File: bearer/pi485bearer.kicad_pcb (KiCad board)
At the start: 2 copper layers, 70 x 30 mm, 23 parts, among them P1 PWR, P2 Rasperry Pi, P3 RO, P4 TERM, P5 CONN_01X04, P6 CONN_01X04, Q1 2N3904, Q2 2N3904, Q3 2N3904, Q4 2N3906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

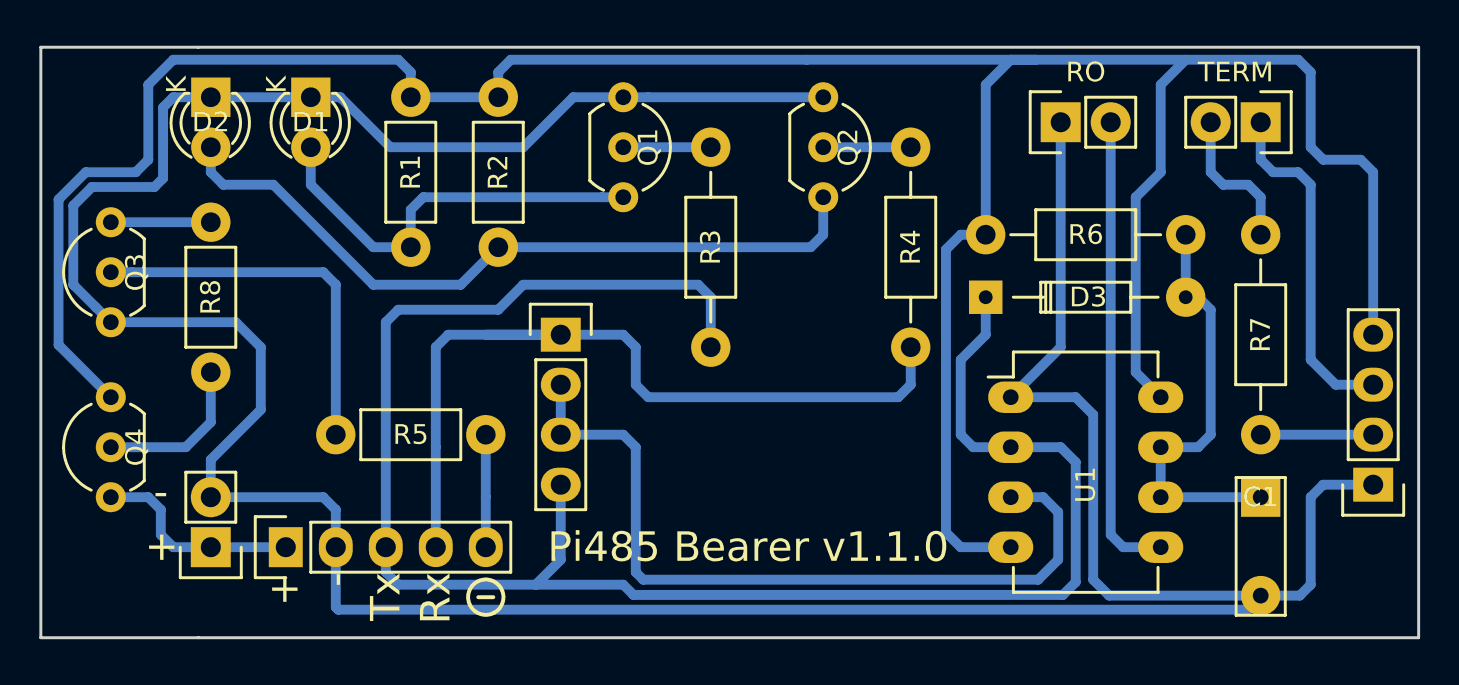
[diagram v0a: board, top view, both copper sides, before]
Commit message: Increased trace size, clearance for PCB etching / printability.
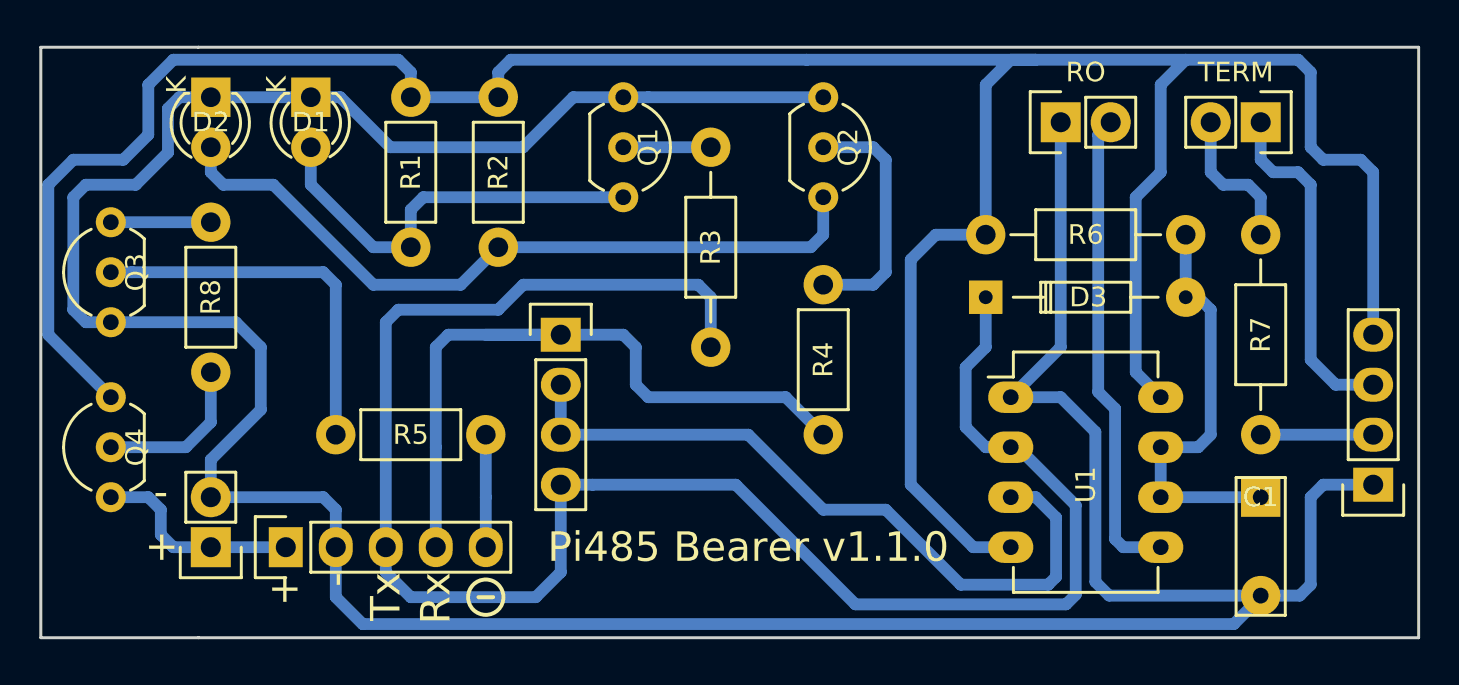
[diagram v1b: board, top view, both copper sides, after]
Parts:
- R4: footprint Resistors_THT:Resistor_Horizontal_RM10mm -> Resistors_THT:Resistor_Horizontal_RM7mm
- moved R4 8.28 mm to (69.2, 33.0)
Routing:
- net Net-(Q2-Pad2): track 4.44 -> 12.6 mm
- net /(RXDO)_GPIO15: track 43.0 -> 37.1 mm
- net /lctec485/DE: track 40.1 -> 36.8 mm
- net /lctec485/VCIN: track 148.7 -> 151.0 mm
- net /(TXDO)_GPIO14: track 94.2 -> 94.9 mm
- net Net-(P3-Pad2): track 23.8 -> 24.3 mm
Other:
- net class Default: clearance 0.25 -> 0.4; trace_width 0.5 -> 0.6
- rule trace_clearance: 0.25 -> 0.4
- rule trace_min: 0.5 -> 0.6

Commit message: 1.1.1 schematics, trace plots, etc.
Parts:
- added C2: 10nF, Capacitors_THT:C_Rect_L4_W2.5_P2.5, F.Cu at (81.3, 34.9)
- added R9: 4.7k, Resistors_THT:Resistor_Horizontal_RM15mm, F.Cu at (74.3, 38.5)
- C1: footprint Capacitors_THT:C_Rect_L7_W2.5_P5 -> Capacitors_THT:C_Rect_L4_W2.5_P2.5
- moved P3 2.84 mm to (83.8, 23.5), turned to 270 degrees
- moved R6 2.54 mm to (87.6, 27.9)
- moved D3 1.90 mm to (77.5, 31.8)
- moved P4 1.27 mm to (91.4, 23.5)
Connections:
- P3 pad 1: GND -> Net-(C2-Pad2)
- P3 pad 2: Net-(P3-Pad2) -> GND
- U1 pad 5: Net-(P3-Pad2) -> Net-(C2-Pad2)
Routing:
- net Net-(P3-Pad2): track 24.3 -> 0.00 mm
- net Net-(C2-Pad2): track 0.00 -> 24.1 mm
- net /lctec485/DE: track 36.8 -> 44.1 mm
- net GND: track 174.4 -> 178.4 mm
- net Net-(C1-Pad1): track 21.5 -> 23.4 mm
- net /(TXDO)_GPIO14: track 94.9 -> 96.6 mm
- net /lctec485/B: track 17.6 -> 18.1 mm
- net Net-(P4-Pad2): track 7.51 -> 8.04 mm
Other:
- net class Default: clearance 0.4 -> 0.5
- rule trace_clearance: 0.4 -> 0.5
- board text added: "Pi485 Bearer v1.1.1"
- board text removed: "Pi485 Bearer v1.1.0"

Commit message: Updates for jumpered biasing on standalone boards. The silly bearer modules you can just unsolder the biasing resistors if it becomes an issue. I should probably add jumpering for that too, but at this point, I just don't much care. A slight modification to those silly SMT boards really isn't that hard...
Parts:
- R9: value 4.7k -> 10k
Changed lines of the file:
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@@
     (links 48)
     (no_connects 0)
-    (area 29.044999 20.789999 101.0875 51.030001)
+    (area 29.389999 20.879999 99.540001 51.030001)
     (thickness 1.6)
     (drawings 27)
@@
       (effects (font (size 1 1) (thickness 0.15)))
     )
-    (fp_text value 4.7k (at 7.38 -1.905 90) (layer F.Fab)
-      (effects (font (size 1 1) (thickness 0.15)))
-    )
+    (fp_text value 10k (at 7.38 -1.905 90) (layer F.Fab)
+      (effects (font (size 1 1) (thickness 0.15)))
+    )
